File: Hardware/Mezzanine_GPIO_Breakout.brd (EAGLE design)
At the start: 30.5 x 44.5 mm, 14 parts, among them U2 EDISON_CONNECTOR_FULLMOUNTING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, U3 EDISON_CONNECTOR_FULLHEADER

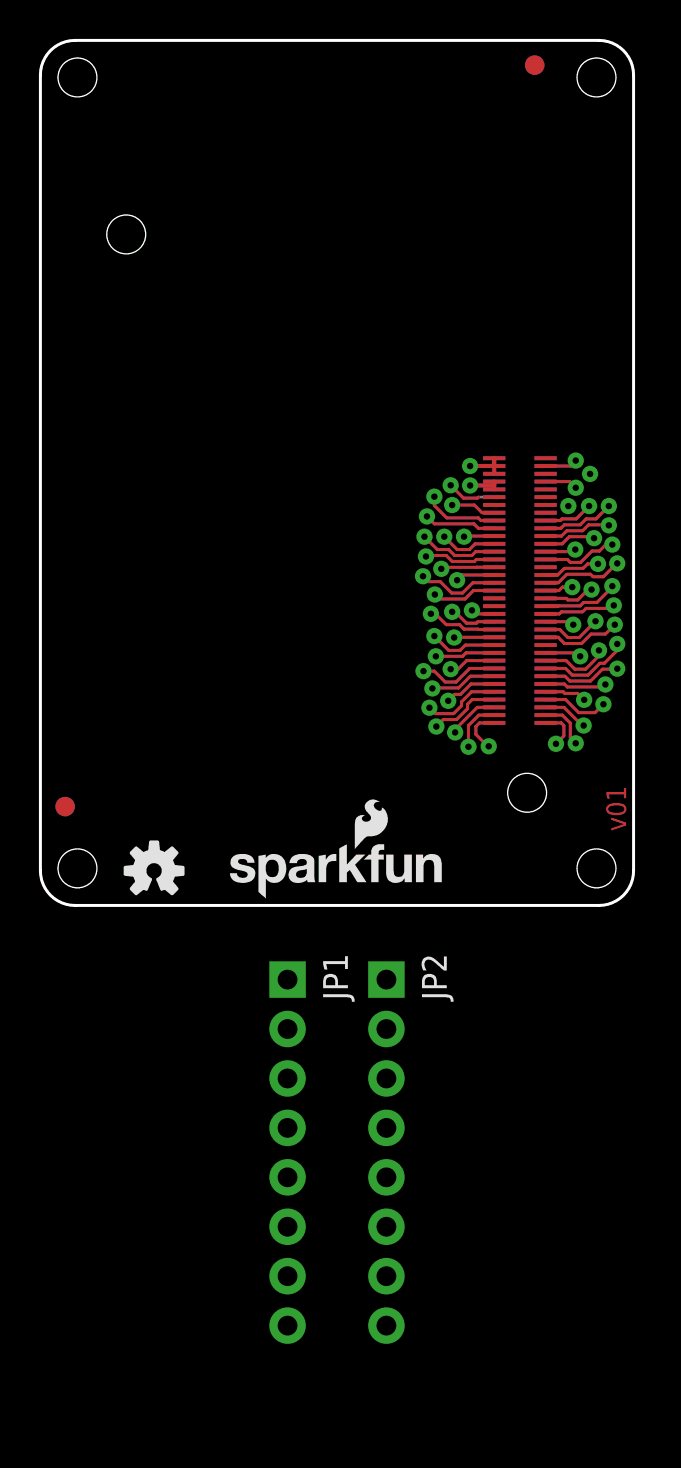
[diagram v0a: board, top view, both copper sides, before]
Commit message: completed layout of GPIO Ready for review
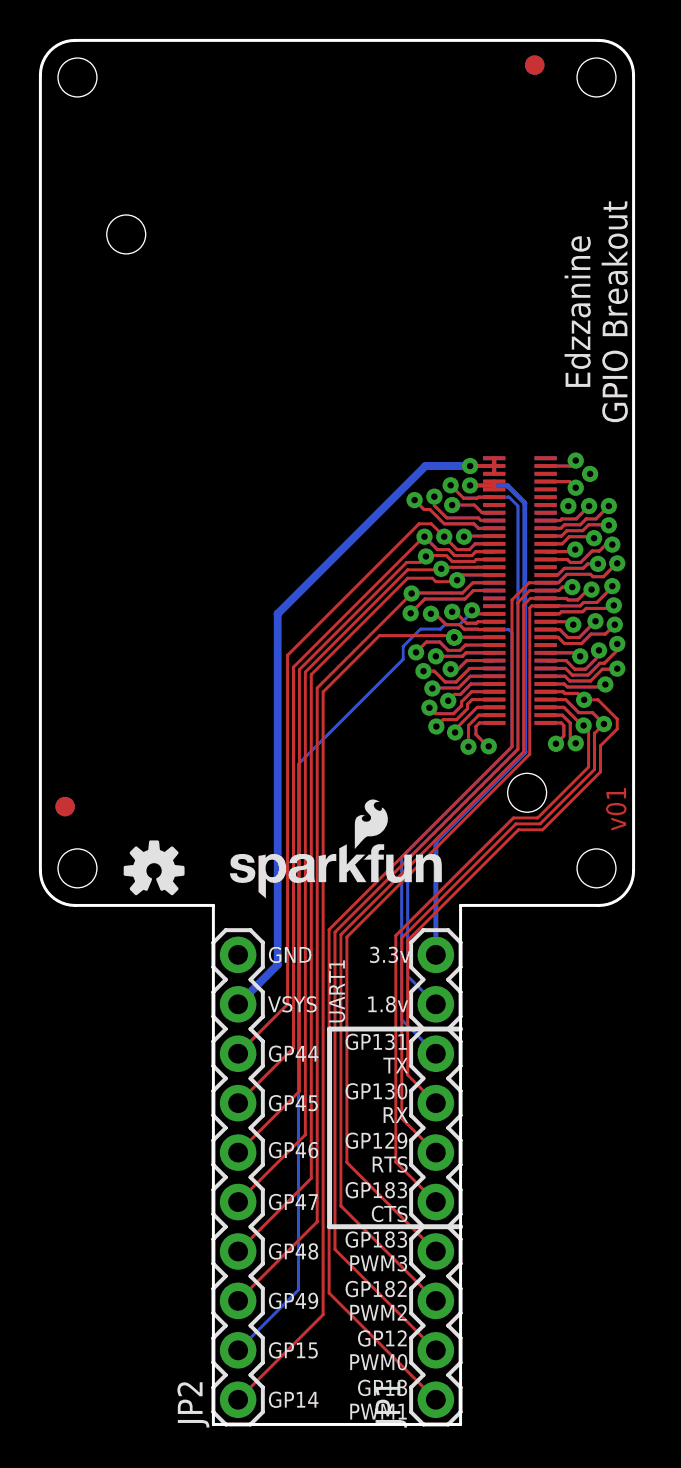
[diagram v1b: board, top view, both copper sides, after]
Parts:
- JP1, JP2: value (none) -> M10"; device SparkFun-Connectors:1X08_PIN1_NO_SILK -> SparkFun-Connectors:1X10
- moved JP1 22.9 mm to (20.3, -25.4), turned to 90 degrees
- moved JP2 22.9 mm to (10.2, -25.4), turned to 90 degrees
- moved FRAME1 20.3 mm to (-1.27, -34.3)
- moved FRAME2 20.3 mm to (-1.27, -34.3)
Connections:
- net 1.8V: now also JP1.9
- net 3.3V: now also JP1.10
- net GND: now also JP2.10
- net GP128_UART_1_CTS: now also JP1.5
- net GP129_UART_1_RTS: now also JP1.6
- net GP12_PWM0: now also JP1.2
- net GP130_UART_1_RX: now also JP1.7
- net GP131_UART_1_TX: now also JP1.8
- net GP13_PWM1: now also JP1.1
- net GP14: now also JP2.1
- net GP15: now also JP2.2
- net GP182_PWM2: now also JP1.3
- net GP183_PWM3: now also JP1.4
- net GP44: now also JP2.8
- net GP45: now also JP2.7
- net GP46: now also JP2.6
- net GP47: now also JP2.5
- net GP48: now also JP2.4
- net GP49: now also JP2.3
- net VSYS: now also JP2.9
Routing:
- net GP13_PWM1: track 8.40 -> 57.8 mm
- net GP14: track 4.13 -> 50.3 mm, vias 1 -> 2
- net GP12_PWM0: track 2.89 -> 49.0 mm
- net GP15: track 2.44 -> 46.5 mm
- net GP182_PWM2: track 5.23 -> 48.2 mm
- net GP48: track 4.04 -> 44.9 mm
- net GP49: track 8.47 -> 49.0 mm
- net GP183_PWM3: track 7.77 -> 47.5 mm
- net GP47: track 5.51 -> 43.4 mm
- net GP46: track 7.39 -> 42.4 mm
- net VSYS: track 4.48 -> 38.4 mm
- net GP45: track 8.13 -> 41.2 mm
- net GP44: track 5.93 -> 38.6 mm
- net 1.8V: track 4.25 -> 35.0 mm
- net GP128_UART_1_CTS: track 4.68 -> 35.0 mm
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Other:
- board size 30.5 x 44.5 mm -> 30.5 x 71.1 mm
- board text added: "1.8v"
- board text added: "3.3v"
- board text added: "Edzzanine GPIO Breakout"
- board text added: "GND"
- board text added: "GP12 PWM0"
- board text added: "GP129 RTS"
- board text added: "GP13 PWM1"
- board text added: "GP130 RX"
- board text added: "GP131 TX"
- board text added: "GP14"
- board text added: "GP15"
- board text added: "GP182 PWM2"
- board text added: "GP183 CTS"
- board text added: "GP183 PWM3"
- board text added: "GP44"
- board text added: "GP45"
- board text added: "GP46"
- board text added: "GP47"
- board text added: "GP48"
- board text added: "GP49"
- board text added: "UART1"
- board text added: "VSYS"
- board text removed: "Example Name of Board"
